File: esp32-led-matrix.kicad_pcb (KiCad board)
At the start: 2 copper layers, 46 x 91 mm, 147 parts, among them J2 Conn_01x04, J4 USB_C_Receptacle_USB2.0_16P, SW1 RESET, U1 ESP32-C6-WROOM-1, U2 USBLC6-2SC6, U3 LM1117DT-3.3

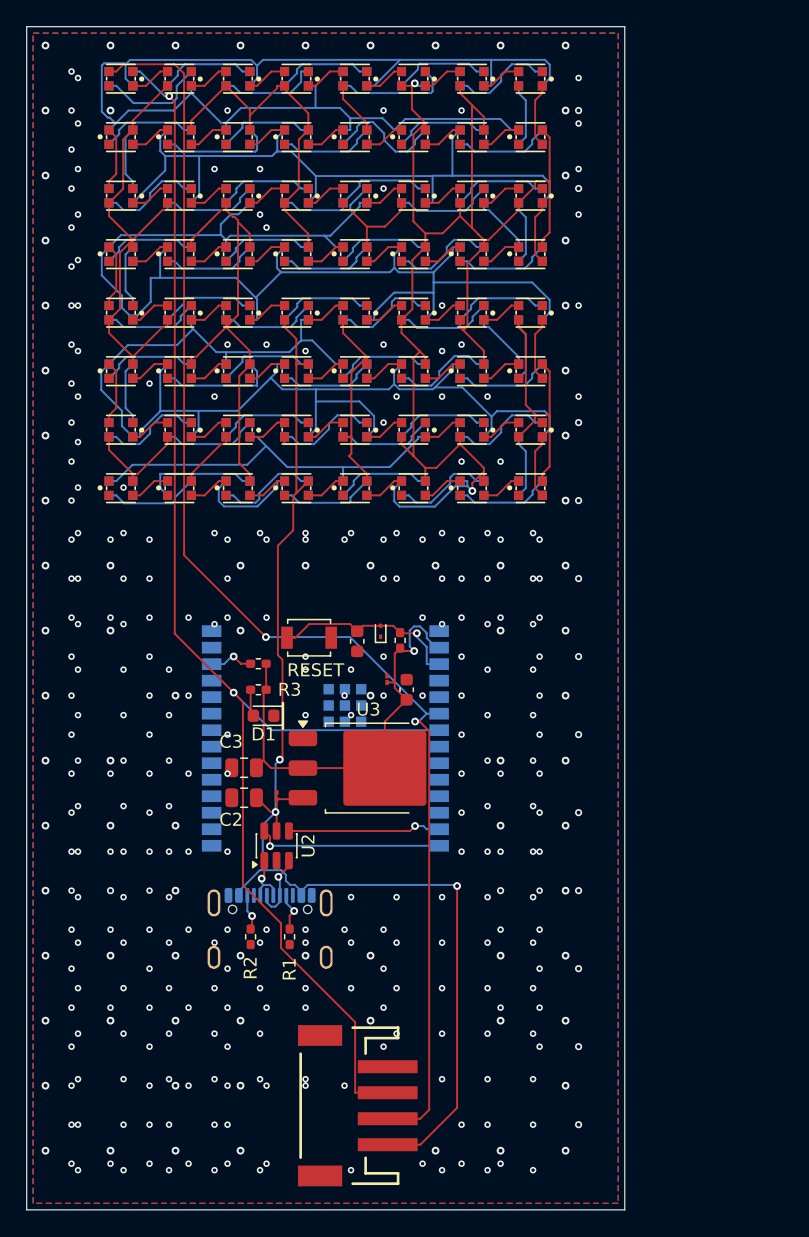
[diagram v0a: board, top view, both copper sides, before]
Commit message: Move board outline and both LED matrices to new compact layout positions (routing intentionally broken, fixed in later task)
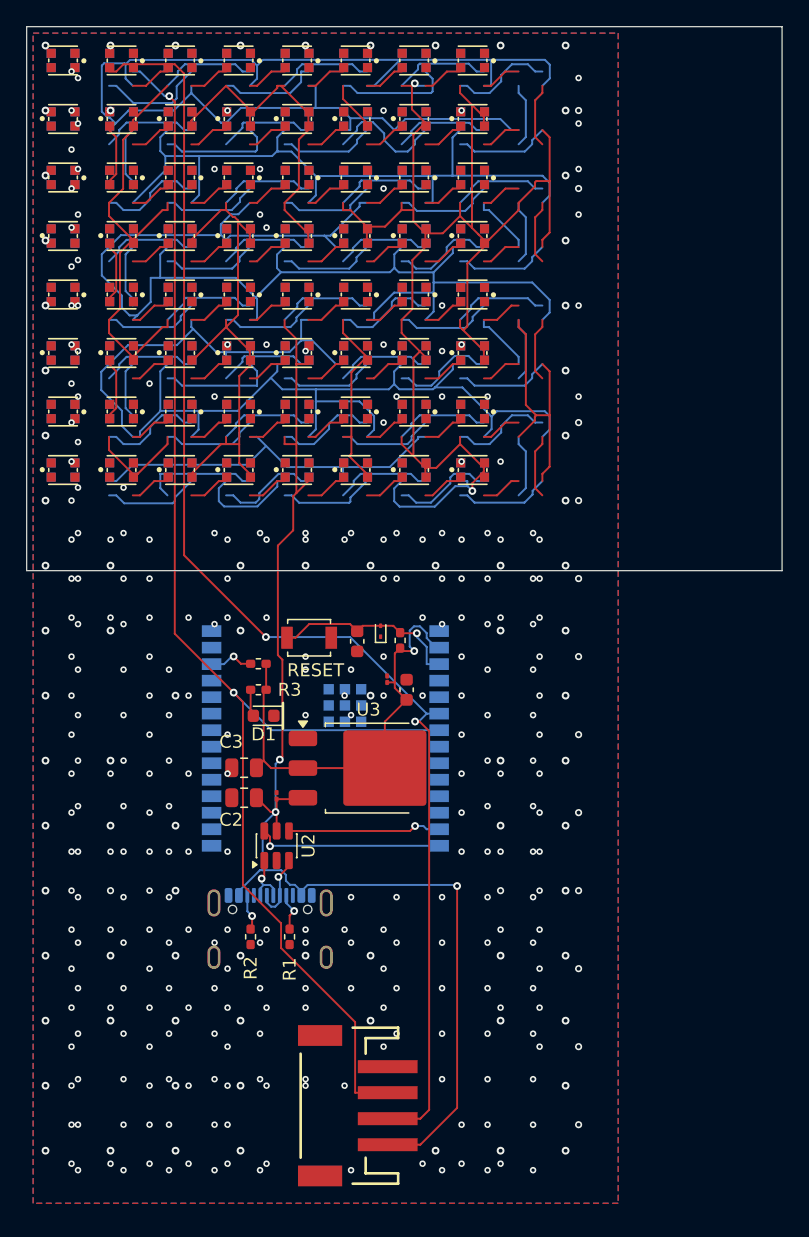
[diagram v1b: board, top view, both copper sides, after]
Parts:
- moved D114 36.0 mm to (2.80, 25.1)
- moved D130 36.0 mm to (2.80, 34.1)
- moved D18 36.0 mm to (2.80, 7.10)
- moved D34 36.0 mm to (2.80, 16.1)
- moved D50 36.0 mm to (2.80, 25.1)
- moved D66 36.0 mm to (2.80, 34.1)
- moved D82 36.0 mm to (2.80, 7.10)
- moved D98 36.0 mm to (2.80, 16.1)
- moved D105 27.1 mm to (34.3, 16.1)
- moved D121 27.1 mm to (34.3, 25.1)
- moved D137 27.1 mm to (34.3, 34.1)
- moved D25 27.1 mm to (34.3, 7.10)
- moved D41 27.1 mm to (34.3, 16.1)
- moved D57 27.1 mm to (34.3, 25.1)
- moved D73 27.1 mm to (34.3, 34.1)
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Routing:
- net +5V: track 748.8 -> 837.9 mm
- net GND: track 0.00 -> 75.0 mm
- net Net-(D66-DOUT): track 3.13 -> 11.5 mm
- net Net-(D111-DOUT): track 7.47 -> 0.00 mm
- net Net-(D95-DOUT): track 7.47 -> 0.00 mm
- net Net-(D96-DOUT): track 7.40 -> 0.00 mm
- net Net-(D112-DOUT): track 7.40 -> 0.00 mm
- net Net-(D63-DOUT): track 3.13 -> 0.00 mm
- net Net-(D62-DOUT): track 3.13 -> 0.00 mm
- net Net-(D61-DOUT): track 3.13 -> 0.00 mm
- net Net-(D60-DOUT): track 3.13 -> 0.00 mm
- net Net-(D59-DOUT): track 3.13 -> 0.00 mm
- net Net-(D58-DOUT): track 3.13 -> 0.00 mm
- net Net-(D56-DOUT): track 3.13 -> 0.00 mm
- net Net-(D55-DOUT): track 3.13 -> 0.00 mm
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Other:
- board size 46 x 91 mm -> 58.1 x 41.8 mm

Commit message: Reposition ESP32-C6 module and verify antenna keepout zone follows it correctly
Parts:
- U1: moved to F.Cu
- moved U1 44.3 mm to (46.9, 17.4), turned to 0 degrees
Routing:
- net LEDB_DATA: track 105.7 -> 108.8 mm
- net unconnected-(U1-GPIO10-Pad11): track 0.00 -> 3.13 mm
- net Net-(D48-DOUT): track 3.13 -> 0.00 mm
- net Net-(D34-DOUT): track 3.13 -> 0.00 mm

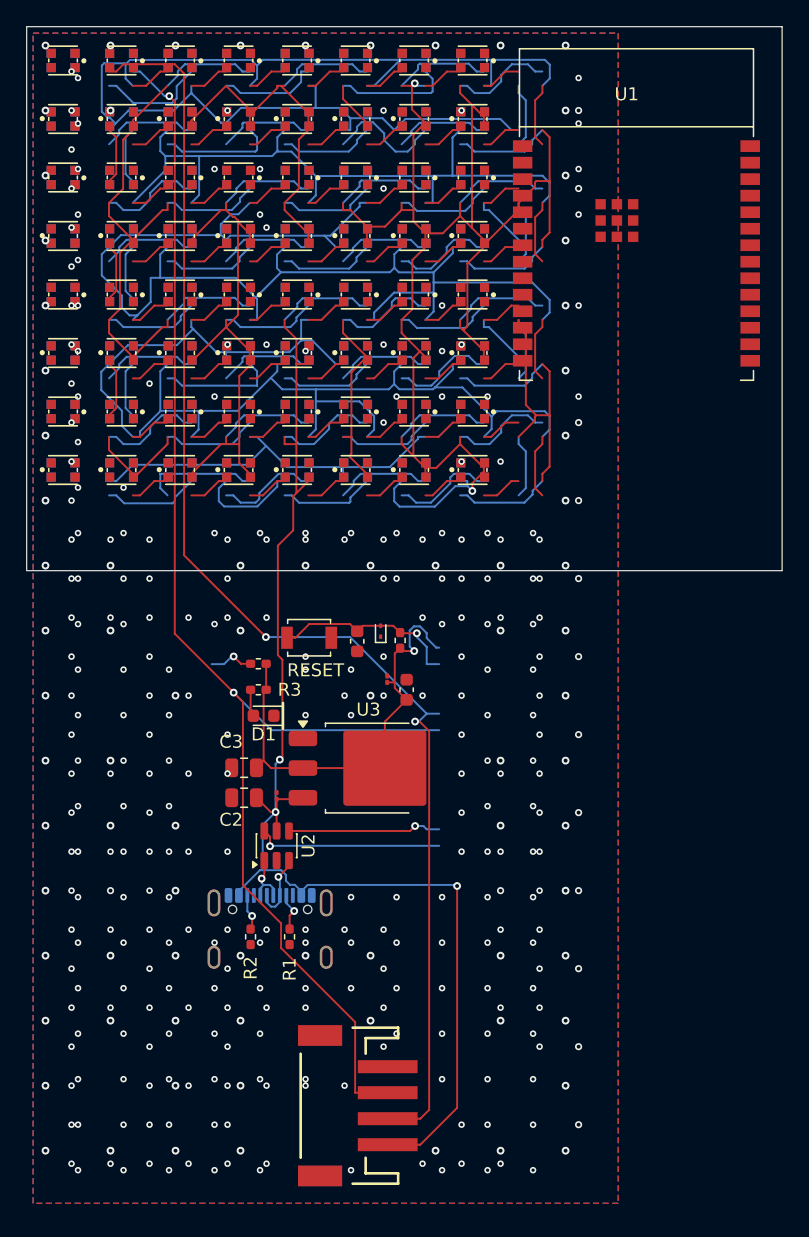
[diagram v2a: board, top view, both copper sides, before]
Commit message: Reposition USB-C (right edge), JST (bottom edge), and remaining B.Cu components per approved layout
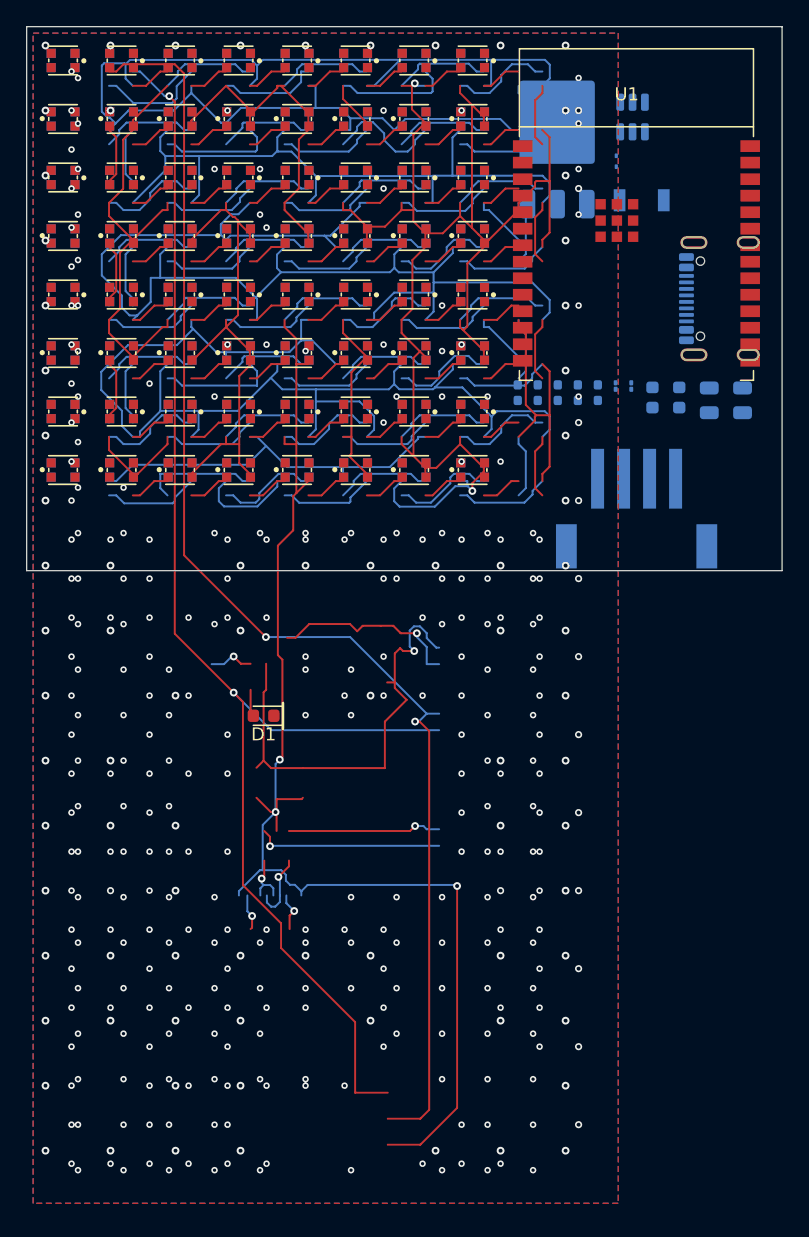
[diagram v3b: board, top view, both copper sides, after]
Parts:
- C1, C2, C3, C4, C5, C6, D4, J2, R1, R2, R3, R7, R8, SW1, U2, U3: moved to B.Cu
- moved U2 62.4 mm to (46.6, 6.95)
- moved J4 61.1 mm to (54.4, 20.9), turned to -90 degrees
- moved U3 50.5 mm to (40.8, 8.61), turned to 90 degrees
- moved J2 49.6 mm to (46.9, 39.5), turned to 0 degrees
- moved C3 47.6 mm to (55.1, 28.7), turned to 90 degrees
- moved R2 47.3 mm to (39.3, 28.1), turned to 90 degrees
- moved C2 47.1 mm to (52.5, 28.7), turned to 90 degrees
- moved R1 45.4 mm to (37.8, 28.1), turned to 90 degrees
- moved SW1 42.3 mm to (47.3, 13.3), turned to 0 degrees
- moved C1 40.9 mm to (45.3, 27.6)
- moved D4 40.4 mm to (45.4, 10.3)
- moved R8 33.4 mm to (43.9, 28.1), turned to 90 degrees
- moved R3 32.4 mm to (40.9, 28.1), turned to 90 degrees
- moved C5 30.7 mm to (50.2, 28.5)
- moved C4 29.4 mm to (48.1, 28.5), turned to 90 degrees
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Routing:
- net +5V: track 837.9 -> 948.6 mm, vias 5 -> 7
- net LEDB_DATA: track 108.8 -> 3.13 mm, vias 2 -> 0
- net Net-(D114-DOUT): track 7.42 -> 0.00 mm
- net GND: track 75.0 -> 82.4 mm, vias 381 -> 380
- net Net-(D97-DOUT): track 4.96 -> 0.00 mm
- net +3V3: vias 1 -> 2

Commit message: Clear all stale copper (traces/vias/zones) from old layout, ready for fresh routing
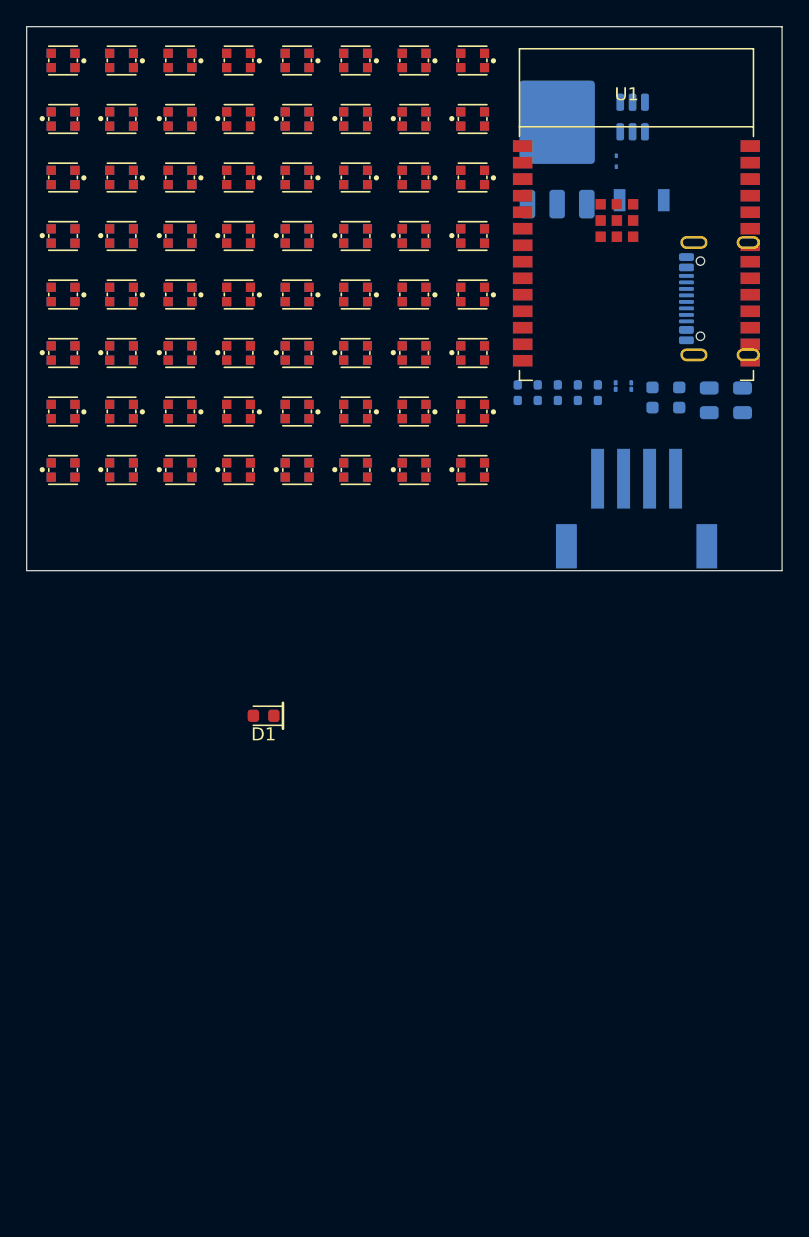
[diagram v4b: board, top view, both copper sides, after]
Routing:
- net +5V: track 948.6 -> 0.00 mm, vias 7 -> 0
- net LEDA_DATA: track 103.1 -> 0.00 mm, vias 2 -> 0
- net GND: track 82.4 -> 0.00 mm, vias 380 -> 0
- net +3V3: track 35.1 -> 0.00 mm, vias 2 -> 0
- net ESP_EN: track 14.7 -> 0.00 mm, vias 1 -> 0
- net USB_D+: track 14.4 -> 0.00 mm, vias 1 -> 0
- net USB_D-: track 11.8 -> 0.00 mm, vias 1 -> 0
- net Net-(D66-DOUT): track 11.5 -> 0.00 mm
- net Net-(D84-DOUT): track 9.30 -> 0.00 mm
- net Net-(D119-DOUT): track 9.00 -> 0.00 mm
- net Net-(D135-DOUT): track 9.00 -> 0.00 mm
- net Net-(D87-DOUT): track 8.93 -> 0.00 mm
- net Net-(D78-DOUT): track 8.93 -> 0.00 mm
- net Net-(D74-DOUT): track 8.44 -> 0.00 mm
- net Net-(D115-DOUT): track 8.05 -> 0.00 mm
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- removed copper zone on B.Cu, net GND
- removed copper zone on F.Cu, net GND

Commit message: Re-route board via Freerouting on new compact layout, add GND/+5V zones
- Added fresh GND/+5V copper pour zones (F.Cu + B.Cu) sized to the new
  57.25 x 41.84mm board outline (0.5mm inset), replicating zone
  settings from commit b6e9c1f (priority, connect_pads=yes,
  clearance=0.3mm, thermal relief 0.3mm) via pcbnew Python API.
  GND kept at priority 1 (wins over +5V priority 0) per the
  priority-bug fix documented in commit 5a5434d.
- Routed all copper via Freerouting. The pre-installed Java-21
  v2.1.0 jar (from a prior session's workaround) reliably found a
  route candidate within seconds but then hung indefinitely in CLI
  mode without ever writing the SES file (matches upstream issue
  freerouting/freerouting#376: -mp / --router.autorouter.max_passes
  does not stop the run in --gui.enabled=false mode on this build).
  Worked around by running Freerouting v2.4.1 (current release, needs
  Java 25) via Docker (eclipse-temurin:25-jre), which completed
  cleanly in ~5 minutes and wrote a valid SES.
- Imported the routed SES: 895 tracks + 34 vias placed, refilled all
  4 zones.
- DRC: 382 violations / 312 unconnected (down from 444 unconnected
  pre-routing). Breakdown: lib_footprint_mismatch=100 (pre-existing,
  benign, documented convention), shorting_items=130 and
  solder_mask_bridge=130 (both concentrated on B.Cu around the tight
  WS2812 LED daisy-chain DOUT/DIN nets -- Freerouting placed routed
  tracks closer than the board's real 0.13mm net-class clearance in
  127/130 cases; 3 are unrelated GND/NC pad proximity carried over
  from task 5's footprint-placement finding), items_not_allowed=9,
  silk_overlap=5, silk_over_copper=4, copper_edge_clearance=2,
  clearance=1, via_dangling=1. 312 unconnected = 174 zone-to-zone
  (same-net F.Cu<->B.Cu stitching-via gaps, not real opens) + 7
  pad-to-zone + 131 genuine net-to-net gaps (5 nets Freerouting
  reported it could not close after 22 passes: GND D1-1->D70-2,
  +3V3 U1-2->U3-2, USB_D+/USB_D- U1<->U2, and Net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
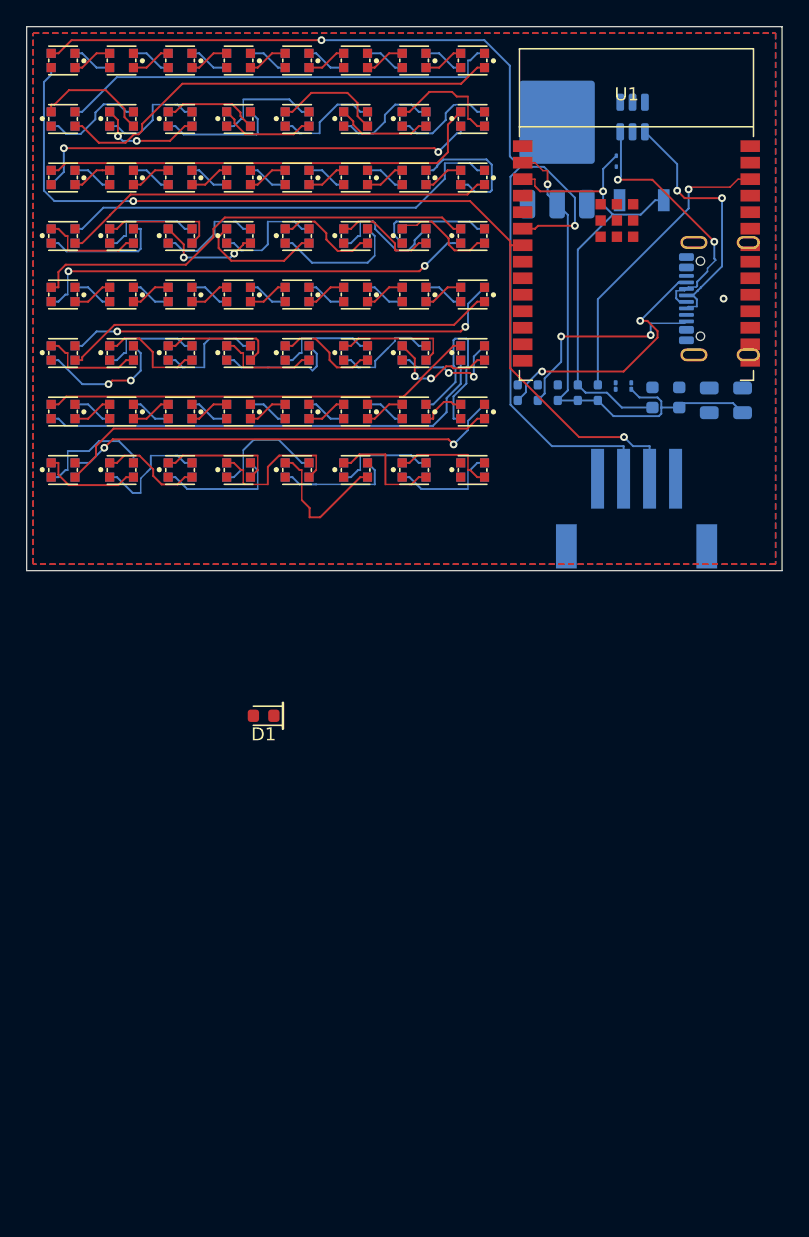
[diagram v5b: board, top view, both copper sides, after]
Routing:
- net LEDA_DATA: track 0.00 -> 87.2 mm, vias 0 -> 2
- net LEDB_DATA: track 0.00 -> 73.6 mm, vias 0 -> 2
- net +3V3: track 0.00 -> 39.7 mm, vias 0 -> 1
- net ESP_EN: track 0.00 -> 37.2 mm, vias 0 -> 1
- net Net-(D121-DOUT): track 0.00 -> 35.5 mm
- net Net-(D41-DOUT): track 0.00 -> 35.2 mm
- net Net-(D89-DOUT): track 0.00 -> 35.0 mm, vias 0 -> 2
- net Net-(D17-DOUT): track 0.00 -> 34.7 mm
- net Net-(D25-DOUT): track 0.00 -> 34.6 mm
- net Net-(D97-DOUT): track 0.00 -> 34.5 mm
- net Net-(D105-DOUT): track 0.00 -> 34.4 mm, vias 0 -> 2
- net Net-(D113-DOUT): track 0.00 -> 34.3 mm, vias 0 -> 2
- net Net-(D81-DOUT): track 0.00 -> 34.1 mm
- net Net-(D129-DOUT): track 0.00 -> 34.1 mm, vias 0 -> 2
- net Net-(D65-DOUT): track 0.00 -> 33.8 mm
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- added copper zone on B.Cu, net +5V
- added copper zone on F.Cu, net +5V
- added copper zone on B.Cu, net GND
- added copper zone on F.Cu, net GND

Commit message: Finalize redesigned compact layout: DRC/ERC cleanup, regenerate fab files and docs, update README
- Fixed stale zone fill from task 6 (Freerouting SES import left GND/+5V
  pours unfilled, causing 382 phantom DRC violations); single ZONE_FILLER
  refill dropped this to 128 baseline violations (100 lib_footprint_mismatch
  + 28 genuine pre-existing issues, documented in README).
- Fixed D1 (power LED) placement bug: was left at y=53mm, outside the
  41.84mm board height (leftover coordinate error from before this redesign
  series). Relocated to a clear F.Cu spot at (51, 36).
- Hand-routed Net-(D79-DOUT) LED daisy-chain gap (0 new violations,
  clearance-verified per segment before committing).
- Added 16 GND stitching vias at verified-clear board locations to reduce
  zone-to-zone pour connectivity gaps.
- Confirmed ERC unchanged from pre-redesign baseline (78 violations,
  byte-identical breakdown) -- schematic was not touched by this PCB-only
  redesign, as expected.
- Regenerated BOM_jlcpcb_verified.csv (16 lines, all LCSC populated, reused
  existing verified numbers, no re-sourcing).
- Regenerated production/ fab package: gerbers.zip (10 files: 6 copper/mask
  layers, edge cuts, drill, drill map, job file), bom.csv, positions.csv
  (148 lines, JLCPCB CPL format) -- all reflect the new 58.1x41.84mm compact
  layout and repositioned components.
- Regenerated docs/images/: schematic.pdf/.png/.svg, pcb-layout.png/.svg,
  and all three 3D renders (top/bottom/isometric) via kicad-cli, showing the
  new compact board.
- Cleaned up docs/images/: removed superseded layout-sketch-proposal v1-v5
  drafts, kept v6 (approved reference design) and _send_* scratch renders.
- Updated README.md Board Specs (new 58.1x41.84mm dimensions, layout
  description), DRC/ERC status (full before/after/final breakdown with
  root-cause analysis and recommended follow-up), and Repo Layout (added
  LAYOUT_SPEC.md).

Final DRC: 128 violations / 189 unconnected (100 lib_footprint_mismatch
ben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
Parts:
- moved D1 36.9 mm to (51.0, 36.0)
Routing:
- net Net-(D81-DOUT): track 34.1 -> 0.00 mm
- net Net-(D117-DOUT): track 9.22 -> 40.5 mm
- net Net-(D129-DOUT): track 34.1 -> 49.8 mm, vias 2 -> 0
- net Net-(D113-DOUT): track 34.3 -> 44.2 mm, vias 2 -> 0
- net Net-(D114-DOUT): track 10.2 -> 3.13 mm, vias 2 -> 0
- net Net-(D102-DOUT): track 10.0 -> 3.13 mm
- net Net-(D109-DOUT): track 3.13 -> 9.80 mm
- net Net-(D78-DOUT): track 3.13 -> 9.77 mm
- net Net-(D103-DOUT): track 9.72 -> 3.13 mm
- net Net-(D131-DOUT): track 9.47 -> 3.10 mm
- net Net-(D132-DOUT): track 9.51 -> 3.17 mm
- net Net-(D124-DOUT): track 3.13 -> 9.44 mm
- net Net-(D111-DOUT): track 3.13 -> 9.44 mm
- net Net-(D130-DOUT): track 9.36 -> 3.10 mm
- net Net-(D90-DOUT): track 3.13 -> 9.33 mm
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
